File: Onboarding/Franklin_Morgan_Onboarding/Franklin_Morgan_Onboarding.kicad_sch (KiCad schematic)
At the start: 0 parts

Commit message: 555 and Potentiometer
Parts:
- added RV1: R_Potentiometer_US, symbol Device:R_Potentiometer_US
- added U1: NE555P, Package_DIP:DIP-8_W7.62mm, symbol Timer:NE555P
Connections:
- new net: RV1.3, U1.2 (TRIG), U1.6 (THRES)
- new net: RV1.2, U1.7 (DISCH)
- new net: RV1.1, U1.8 (VCC)

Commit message: Schematic Finish
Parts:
- added C1: C_US, Package_DFN_QFN:QFN-32-1EP_5x5mm_P0.5mm_EP3.6x3.6mm_ThermalVias, symbol Device:C_US
- added C2: C_US, symbol Device:C_US
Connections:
- net GND: now also U1.1 (GND), C1.2
- net at RV1.3, U1.2 (TRIG), U1.6 (THRES): now also C1.1
- net +5V: now reaches U1.4 (~{RST})
- net +5V: now also RV1.1, U1.8 (VCC), C2.1
- net at U1.5 (CONT): now also C2.2

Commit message: Schematic Update
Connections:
- no-connect marks 0 -> 1
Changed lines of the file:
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@@
+	)
+	(junction
+		(at 110.49 73.66)
+		(diameter 0)
+		(color 0 0 0 0)
 	)
 	(junction
@@
 	)
 	(junction
+		(at 123.19 38.1)
+		(diameter 0)
+		(color 0 0 0 0)
+	)
+	(junction
 		(at 130.81 38.1)
 		(diameter 0)
@@
 		(color 0 0 0 0)
 	)
+	(no_connect
+		(at 140.97 55.88)
+	)
 	(wire
 		(pts
@@
 	(wire
 		(pts
+			(xy 110.49 73.66) (xy 110.49 71.12)
+		)
+		(stroke
+			(width 0)
+			(type default)
+		)
+	)
+	(wire
+		(pts
 			(xy 120.65 58.42) (xy 120.65 60.96)
 		)
@@
 		(pts
 			(xy 110.49 63.5) (xy 120.65 63.5)
+		)
+		(stroke
+			(width 0)
+			(type default)
+		)
+	)
+	(wire
+		(pts
+			(xy 110.49 78.74) (xy 110.49 73.66)
 		)
 		(stroke
@@
 	(symbol
 		(lib_id "power:GND")
-		(at 110.49 71.12 0)
+		(at 110.49 78.74 0)
 		(unit 1)
 		(body_style 1)
@@
 		(fields_autoplaced yes)
 		(property "Reference" "#PWR01"
-			(at 110.49 77.47 0)
+			(at 110.49 85.09 0)
 			(hide yes)
 			(show_name no)
@@
 		)
 		(property "Value" "GND"
-			(at 110.49 76.2 0)
+			(at 110.49 83.82 0)
 			(show_name no)
 			(do_not_autoplace no)
@@
 		)
 		(property "Footprint" ""
-			(at 110.49 71.12 0)
+			(at 110.49 78.74 0)
 			(hide yes)
 			(show_name no)
@@
 		)
 		(property "Datasheet" ""
-			(at 110.49 71.12 0)
+			(at 110.49 78.74 0)
 			(hide yes)
 			(show_name no)
@@
 		)
 		(property "Description" "Power symbol creates a global label with name \"GND\" , ground"
-			(at 110.49 71.12 0)
+			(at 110.49 78.74 0)
 			(hide yes)
 			(show_name no)
@@
 				(path "/44c49502-c9ff-469b-99f2-8f885cdcdf7f"
 					(reference "#PWR01")
+					(unit 1)
+				)
+			)
+		)
+	)
+	(symbol
+		(lib_id "power:PWR_FLAG")
+		(at 110.49 73.66 90)
+		(unit 1)
+		(body_style 1)
+		(exclude_from_sim no)
+		(in_bom yes)
+		(on_board yes)
+		(in_pos_files yes)
+		(dnp no)
+		(fields_autoplaced yes)
+		(property "Reference" "#FLG02"
+			(at 108.585 73.66 0)
+			(hide yes)
+			(show_name no)
+			(do_not_autoplace no)
+			(effects
+				(font
+					(size 1.27 1.27)
+				)
+			)
+		)
+		(property "Value" "PWR_FLAG"
+			(at 106.68 73.6599 90)
+			(show_name no)
+			(do_not_autoplace no)
+			(effects
+				(font
+					(size 1.27 1.27)
+				)
+				(justify left)
+			)
+		)
+		(property "Footprint" ""
+			(at 110.49 73.66 0)
+			(hide yes)
+			(show_name no)
+			(do_not_autoplace no)
+			(effects
+				(font
+					(size 1.27 1.27)
+				)
+			)
+		)
+		(property "Datasheet" ""
+			(at 110.49 73.66 0)
+			(hide yes)
+			(show_name no)
+			(do_not_autoplace no)
+			(effects
+				(font
+					(size 1.27 1.27)
+				)
+			)
+		)
+		(property "Description" "Special symbol for telling ERC where power comes from"
+			(at 110.49 73.66 0)
+			(hide yes)
+			(show_name no)
+			(do_not_autoplace no)
+			(effects
+				(font
+					(size 1.27 1.27)
+				)
+			)
+		)
+		(pin "1"
+		)
+		(instances
+			(project "Franklin_Morgan_Onboarding"
+				(path "/44c49502-c9ff-469b-99f2-8f885cdcdf7f"
+					(reference "#FLG02")
 					(unit 1)
 				)
@@
 					(unit 1)
 				)
+			)
+		)
+	)
+	(symbol
+		(lib_id "power:PWR_FLAG")
+		(at 123.19 38.1 0)
+		(unit 1)
+		(body_style 1)
+		(exclude_from_sim no)
+		(in_bom yes)
+		(on_board yes)
+		(in_pos_files yes)
+		(dnp no)
+		(fields_autoplaced yes)
+		(property "Reference" "#FLG01"
+			(at 123.19 36.195 0)
+			(hide yes)
+			(show_name no)
+			(do_not_autoplace no)
+			(effects
+				(font
+					(size 1.27 1.27)
+				)
+			)
+		)
+		(property "Value" "PWR_FLAG"
+			(at 123.19 33.02 0)
+			(show_name no)
+			(do_not_autoplace no)
+			(effects
+				(font
+					(size 1.27 1.27)
+				)
+			)
+		)
+		(property "Footprint" "Package_SO:TSSOP-28_4.4x9.7mm_P0.65mm"
+			(at 123.19 38.1 0)
+			(hide yes)
+			(show_name no)
+			(do_not_autoplace no)
+			(effects
+				(font
+					(size 1.27 1.27)
+				)
+			)
+		)
+		(property "Datasheet" ""
+			(at 123.19 38.1 0)
+			(hide yes)
+			(show_name no)
+			(do_not_autoplace no)
+			(effects
+				(font
+					(size 1.27 1.27)
+				)
+			)
+		)
+		(property "Description" "Special symbol for telling ERC where power comes from"
+			(at 123.19 38.1 0)
+			(hide yes)
+			(show_name no)
+			(do_not_autoplace no)
+			(effects
+				(font
+					(size 1.27 1.27)
+				)
+			)
+		)
+		(pin "1"
+		)
+		(instances
+			(project "Franklin_Morgan_Onboarding"
+				(path "/44c49502-c9ff-469b-99f2-8f885cdcdf7f"
+					(reference "#FLG01")
+					(unit 1)
+				)

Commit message: Updated Schematic
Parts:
- added J1: Conn_01x02_Pin, Relay_THT:Relay_DPDT_Schrack-RT2-FormC_RM5mm, symbol Connector:Conn_01x02_Pin
- C1: value C_US -> 0.15pF
- C2: value C_US -> 0.01u F
- RV1: value R_Potentiometer_US -> 1-10k
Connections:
- net +5V: now also J1.1 (Pin_1); no longer C2.1, RV1.1, U1.4 (~{RST}), U1.8 (VCC)
- net GND: now also J1.2 (Pin_2)
- new net: C2.1, RV1.1, U1.4 (~{RST}), U1.8 (VCC)

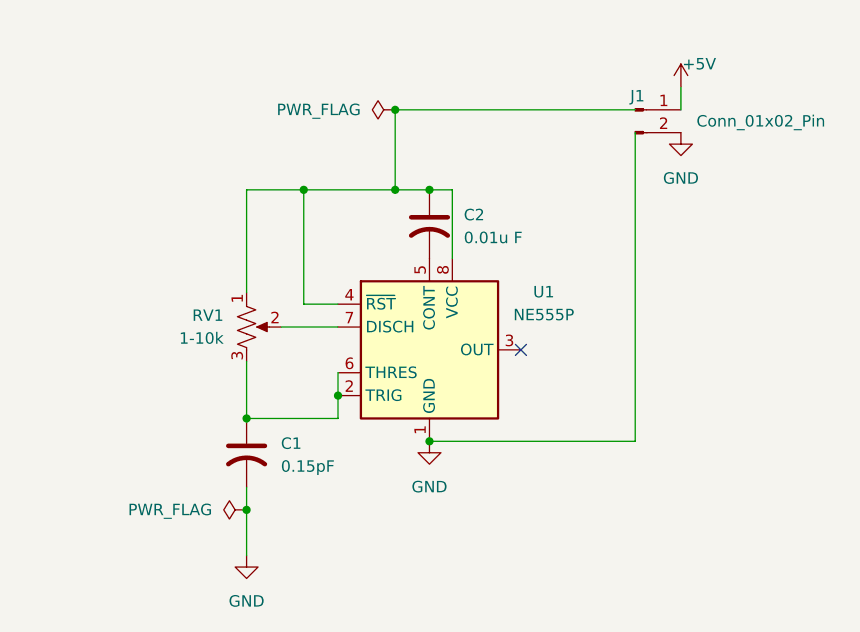
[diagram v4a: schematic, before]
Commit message: Updated Sch and PCB
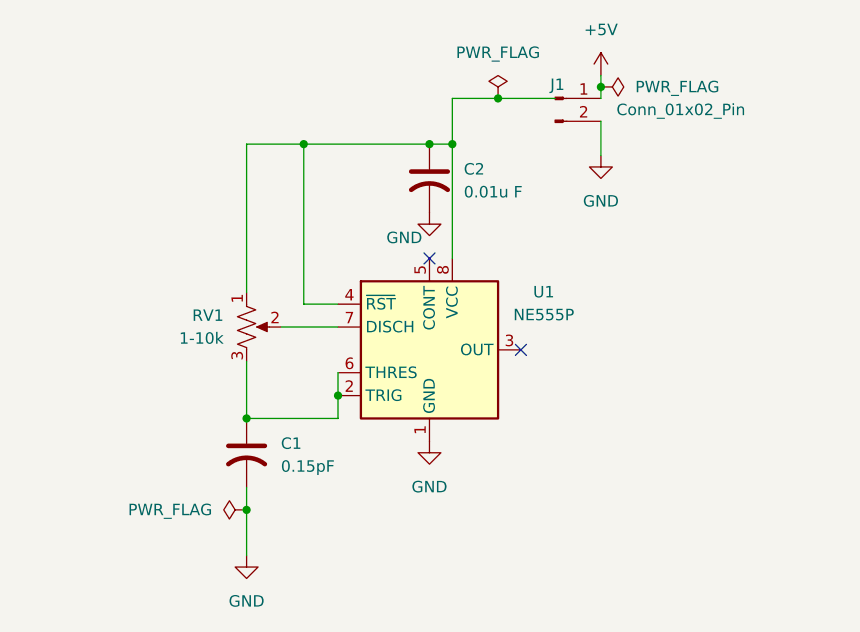
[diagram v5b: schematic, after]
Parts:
- C1: footprint Package_DFN_QFN:QFN-32-1EP_5x5mm_P0.5mm_EP3.6x3.6mm_ThermalVias -> Capacitor_SMD:C_1206_3216Metric
- C2: footprint (none) -> Capacitor_SMD:C_1206_3216Metric
- J1: footprint Relay_THT:Relay_DPDT_Schrack-RT2-FormC_RM5mm -> Connector_PinHeader_2.00mm:PinHeader_1x02_P2.00mm_Vertical
- RV1: footprint (none) -> Potentiometer_THT:Potentiometer_Alps_RK09K_Single_Vertical
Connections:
- net GND: now also C2.2
- net at U1.5 (CONT): no longer C2.2
- no-connect marks 1 -> 2
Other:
- moved on the sheet: C2, J1
